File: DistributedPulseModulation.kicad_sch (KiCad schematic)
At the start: 41 parts, among them J1 Conn_02x12_Odd_Even, J2 Conn_02x05_Odd_Even, U1 74LS251, U2 74LVC2G74, U25 74LS85, U28 74LS85, U3 ADG333A, U31 74LS85, U4 MCP23017_SP, U5 ADG333A, U6 ADG333A, U8 4040, U9 4040

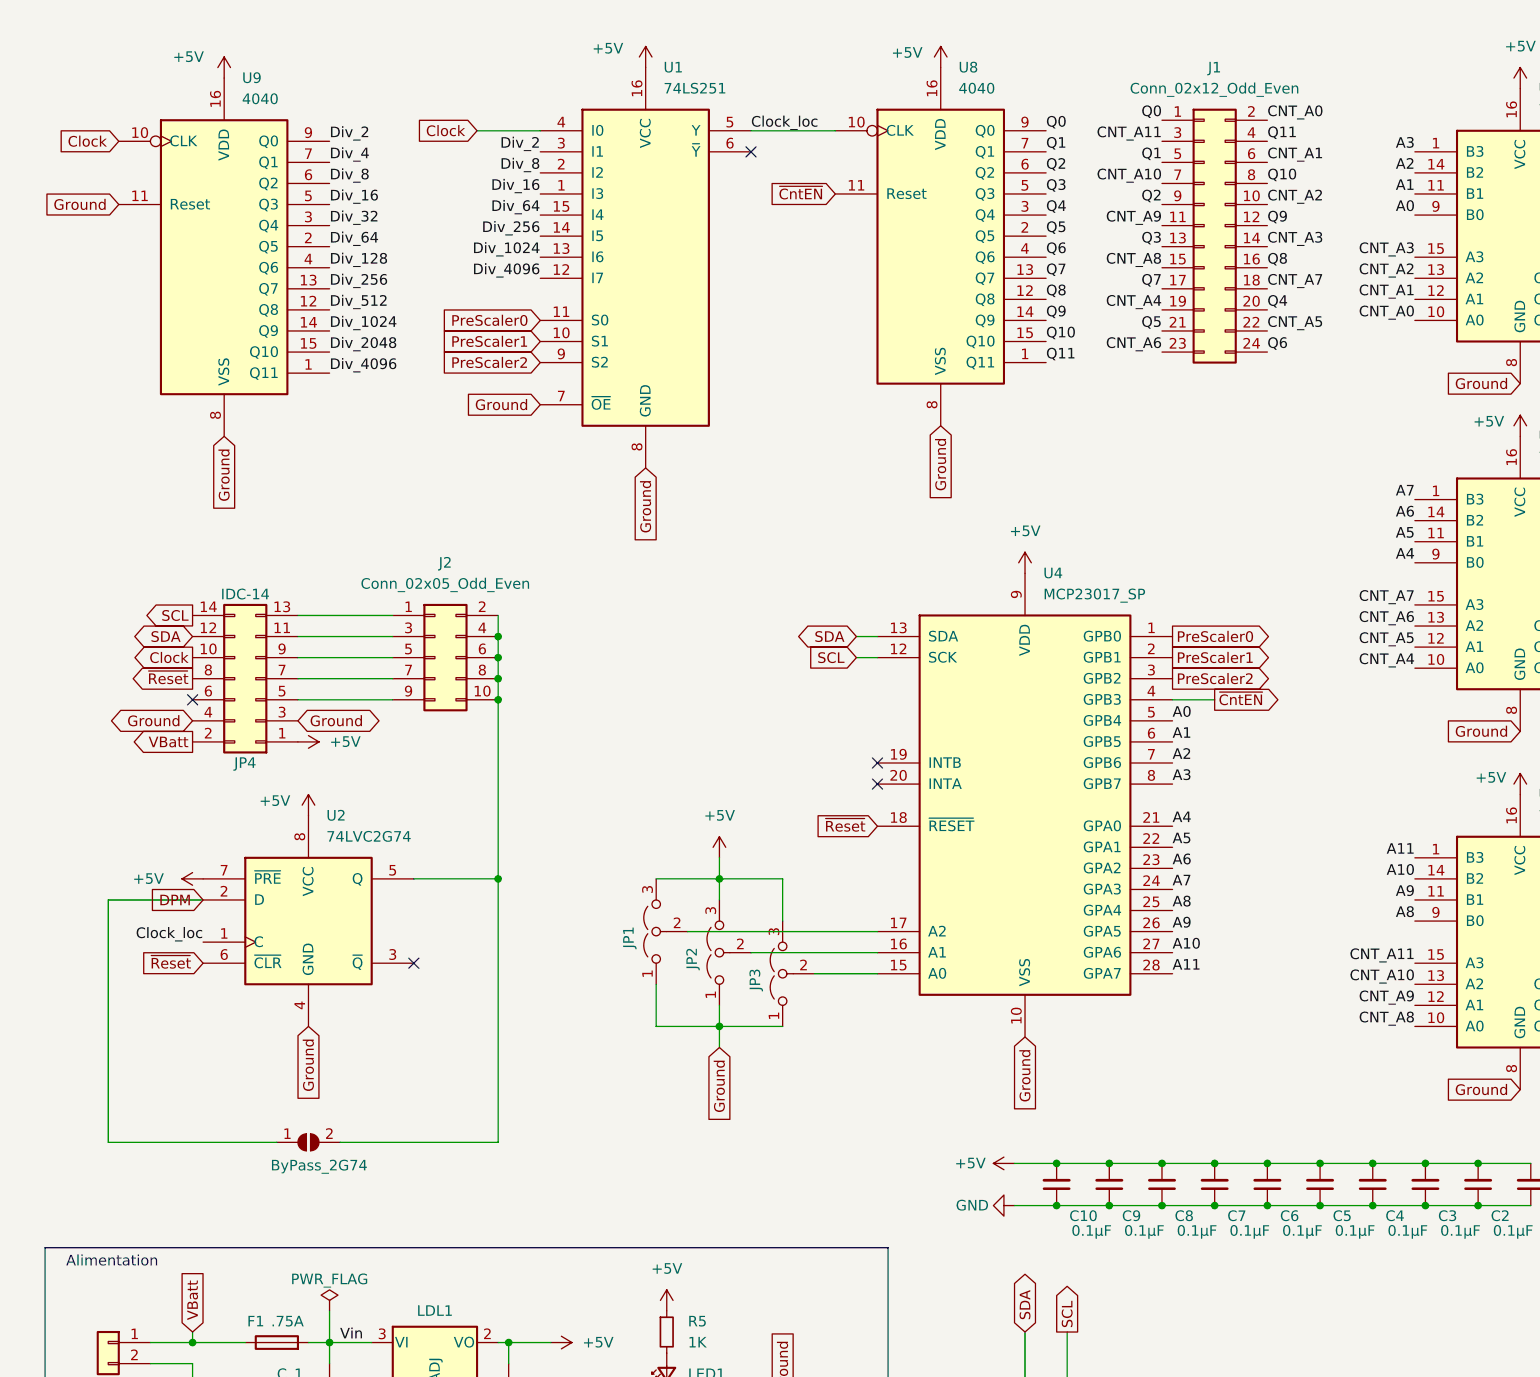
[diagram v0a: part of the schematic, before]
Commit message: RETROFIT : connecteur perso PCIe_CAN pour compatibilité avec le CANduino128 comme microcontôleur maitre
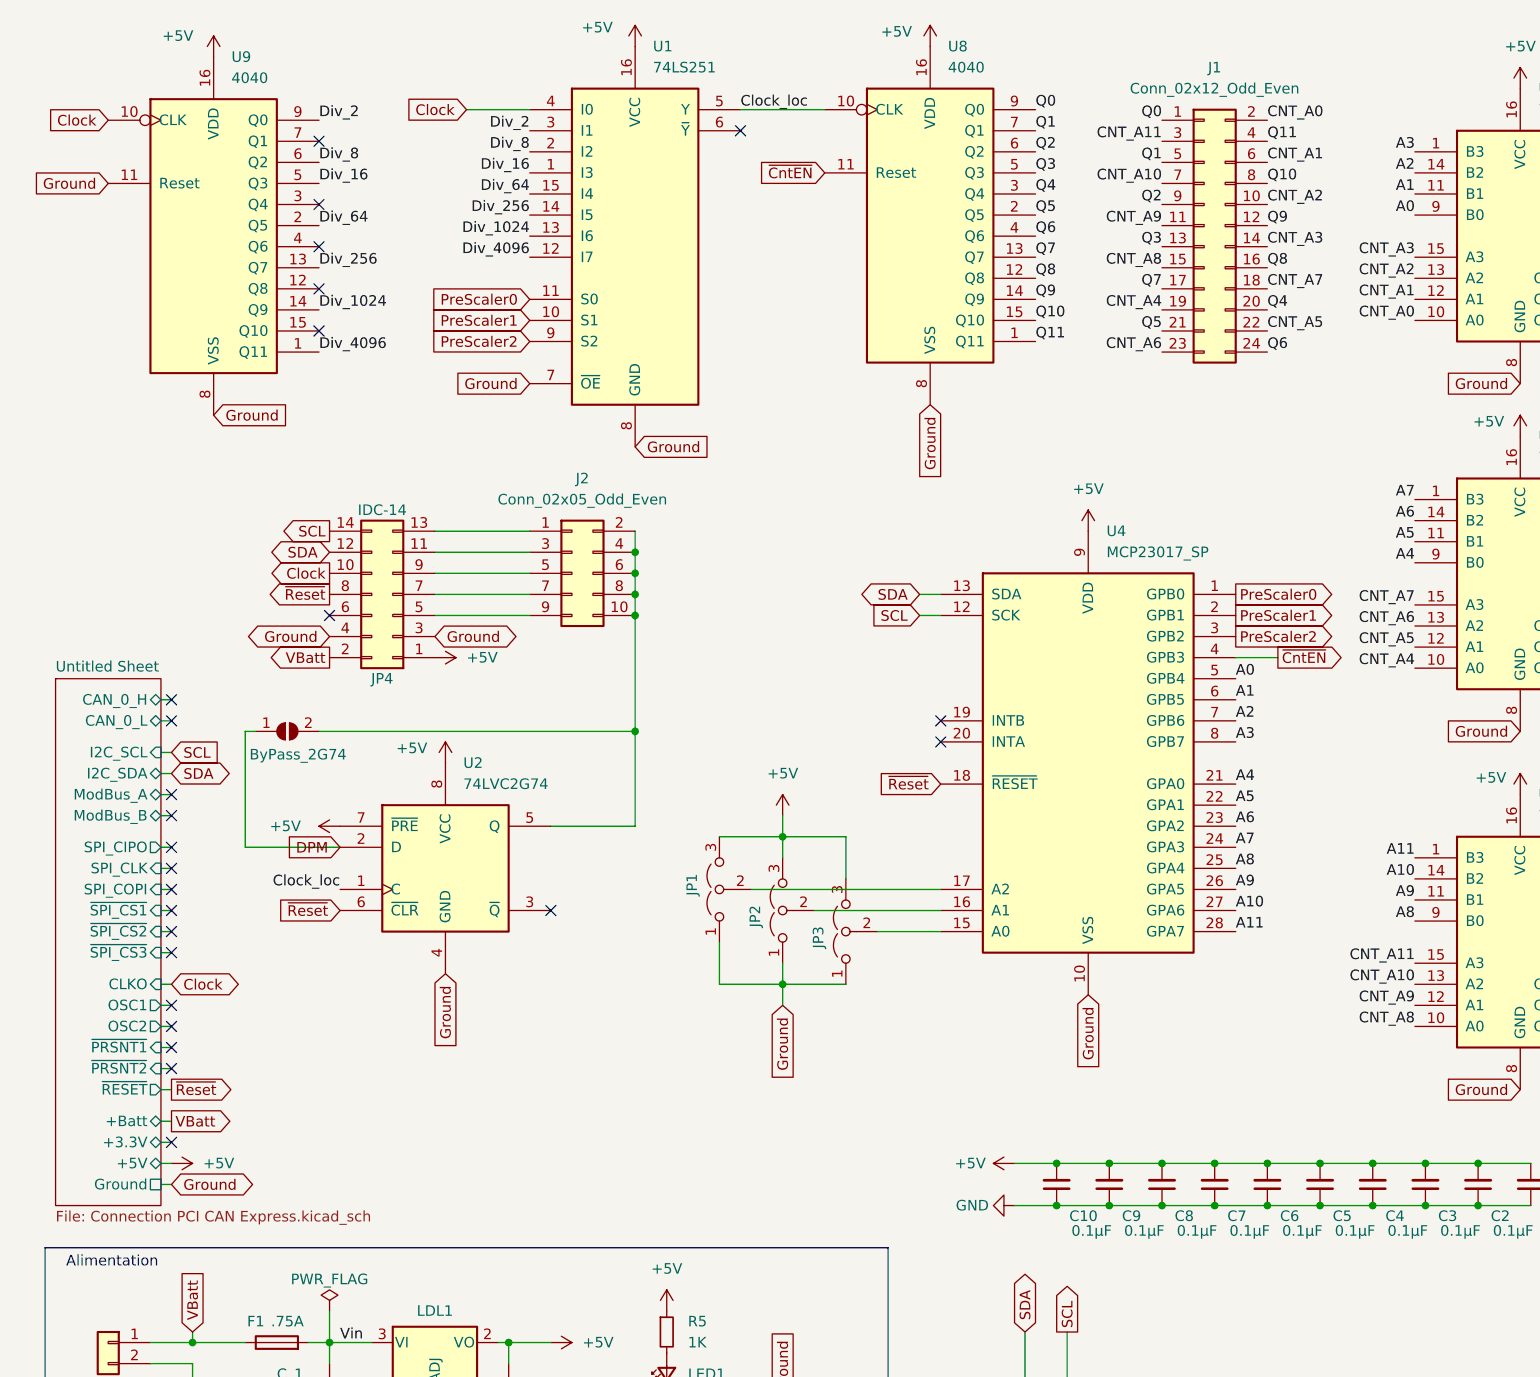
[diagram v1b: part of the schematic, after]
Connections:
- net Div_128: no longer names the net of U9.4 (Q6)
- net Div_2048: no longer names the net of U9.15 (Q10)
- net Div_32: no longer names the net of U9.3 (Q4)
- net Div_4: no longer names the net of U9.7 (Q1)
- net Div_512: no longer names the net of U9.12 (Q8)
- no-connect marks 7 -> 27
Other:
- added sheet Untitled Sheet (Connection PCI CAN Express.kicad_sch)
- moved on the sheet: ByPass_2G74, J2, JP1, JP2, JP3, JP4, U1, U2, U4, U8, U9

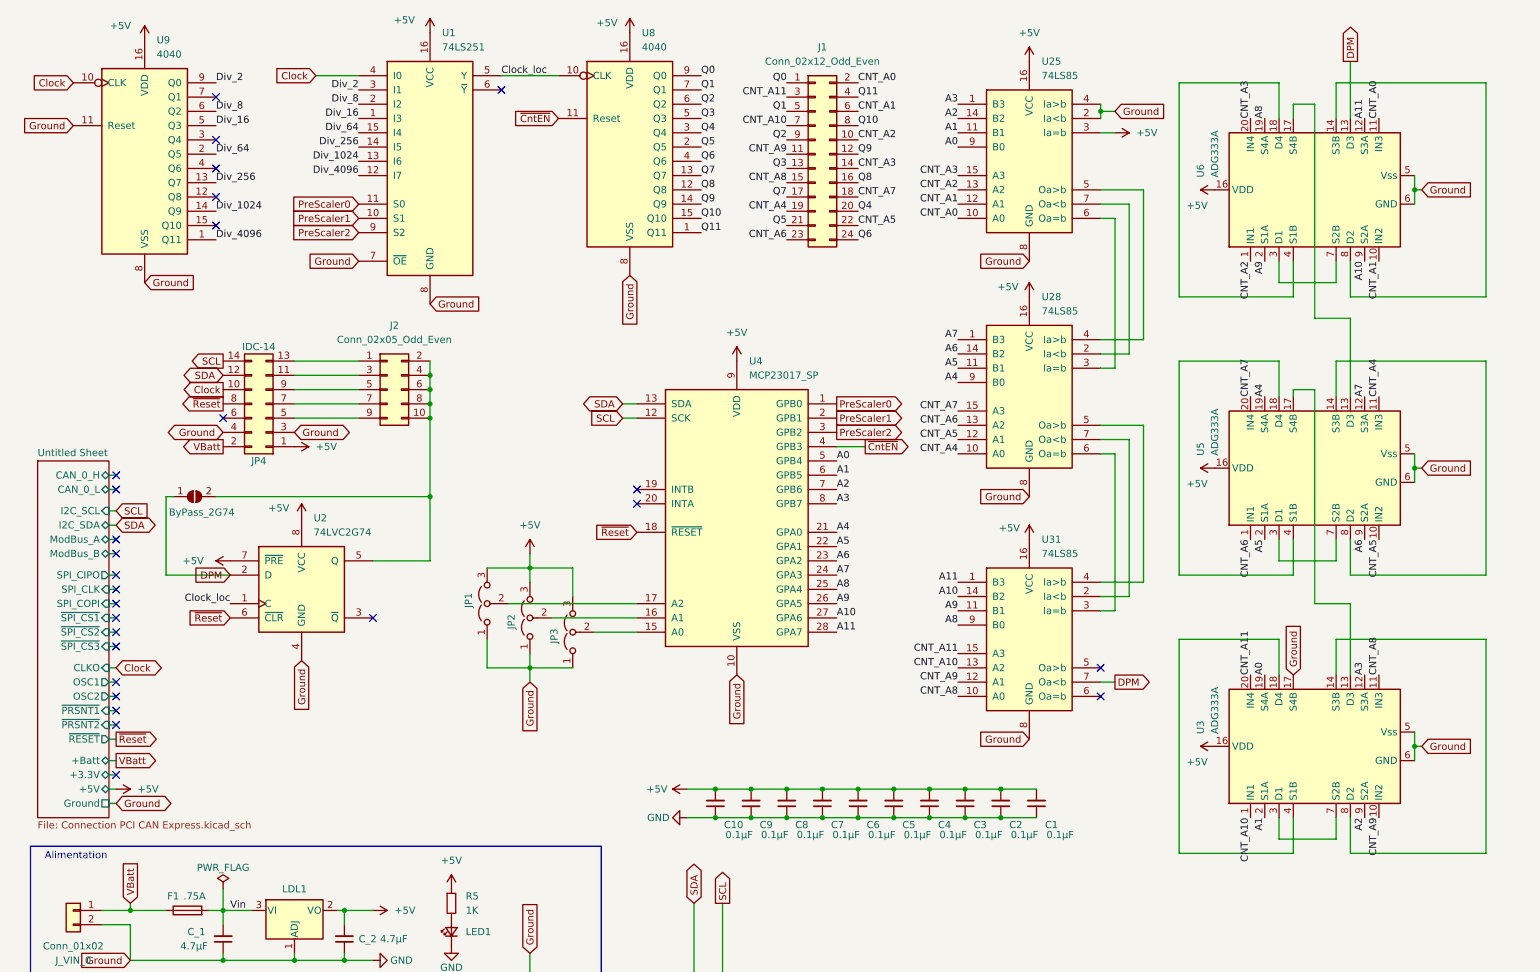
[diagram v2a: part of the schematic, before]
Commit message: Fin de simplification du routage. Génération des Gerber.
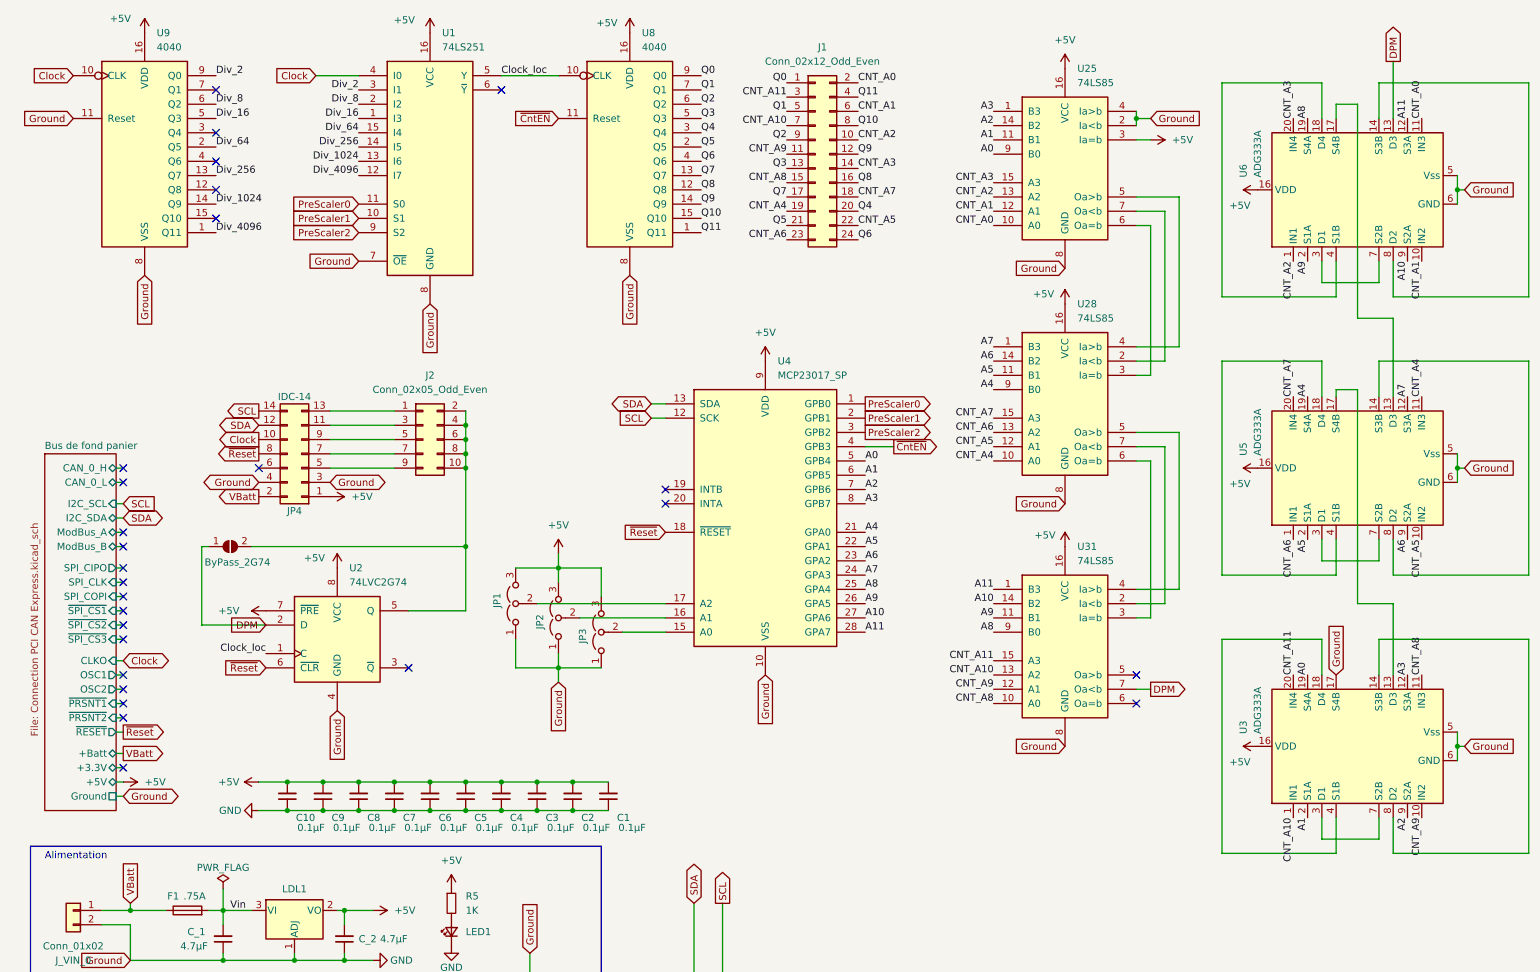
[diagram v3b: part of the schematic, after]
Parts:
- U2: footprint Package_SO_AKL:SSOP-8_2.95x2.8mm_P0.65mm -> Package_SO:SSOP-8_2.95x2.8mm_P0.65mm
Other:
- sheet Untitled Sheet renamed Bus de fond panier
- moved on the sheet: ByPass_2G74, C1, C10, C2, C3, C4, C5, C6, C7, C8, C9, J2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

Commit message: Full rework : ADG333A 10x plus chers que cd74hct4053 Nouveau chips et nouveau routage JPP TT
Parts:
- removed U3, U5, U6: ADG333A, Package_DIP:DIP-20_W7.62mm_Socket_LongPads, symbol Perso_Spare_parts:ADG333A
- added C11: 0.1µF, Capacitor_THT:C_Disc_D5.0mm_W2.5mm_P5.00mm, symbol Device:C_Small
- added U10, U11, U12, U7: 4053, Package_DIP:DIP-16_W7.62mm_Socket, symbol 4xxx:4053
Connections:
- net +5V: now also C11.2, U10.16 (VDD), U11.16 (VDD), U12.16 (VDD), U7.16 (VDD)
- net A0: now also U7.13 (X1)
- net A1: now also U7.1 (Y1)
- net A10: now also U12.1 (Y1)
- net A11: now also U12.3 (Z1)
- net A2: now also U7.3 (Z1)
- net A3: now also U10.13 (X1)
- net A4: now also U10.1 (Y1)
- net A5: now also U10.3 (Z1)
- net A6: now also U11.13 (X1)
- net A7: now also U11.1 (Y1)
- net A8: now also U11.3 (Z1)
- net A9: now also U12.13 (X1)
- net CNT_A0: now also U12.9 (C)
- net CNT_A1: now also U12.10 (B)
- net CNT_A10: now also U7.10 (B)
- net CNT_A11: now also U7.11 (A)
- net CNT_A2: now also U12.11 (A)
- net CNT_A3: now also U11.9 (C)
- net CNT_A4: now also U11.10 (B)
- net CNT_A5: now also U11.11 (A)
- net CNT_A6: now also U10.9 (C)
- net CNT_A7: now also U10.10 (B)
- net CNT_A8: now also U10.11 (A)
- net CNT_A9: now also U7.9 (C)
- net DPM: now also U12.4 (Z)
- net GND: now also C11.1, U10.6 (Inh), U10.7 (VEE), U10.8 (VSS), U11.6 (Inh), U11.7 (VEE), U11.8 (VSS), U12.6 (Inh), U12.7 (VEE), U12.8 (VSS), U7.12 (X0), U7.6 (Inh), U7.7 (VEE), U7.8 (VSS)
- new net: U11.4 (Z), U12.12 (X0)
- new net: U12.14 (X), U12.2 (Y0)
- new net: U12.15 (Y), U12.5 (Z0)
- new net: U7.14 (X), U7.2 (Y0)
- new net: U7.15 (Y), U7.5 (Z0)
- new net: U10.12 (X0), U7.4 (Z)
- new net: U10.14 (X), U10.2 (Y0)
- new net: U10.15 (Y), U10.5 (Z0)
- new net: U10.4 (Z), U11.12 (X0)
- new net: U11.14 (X), U11.2 (Y0)
- new net: U11.15 (Y), U11.5 (Z0)
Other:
- moved on the sheet: ByPass_2G74, C1, C10, C2, C3, C4, C5, C6, C7, C8, C9, C_1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
